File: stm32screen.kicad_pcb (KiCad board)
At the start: 4 copper layers, 49.8 x 49.8 mm, 38 parts, among them J1 SWD, J2 GC9A01, J3 Oil temp sensor, J4 pressure sensor, J5 USB_B_Micro, J6 EGT_sensor, SW1 SW_Push, SW2 SW_Push, U1 TS1117BCW-3.3, U2 STM32F407VETx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

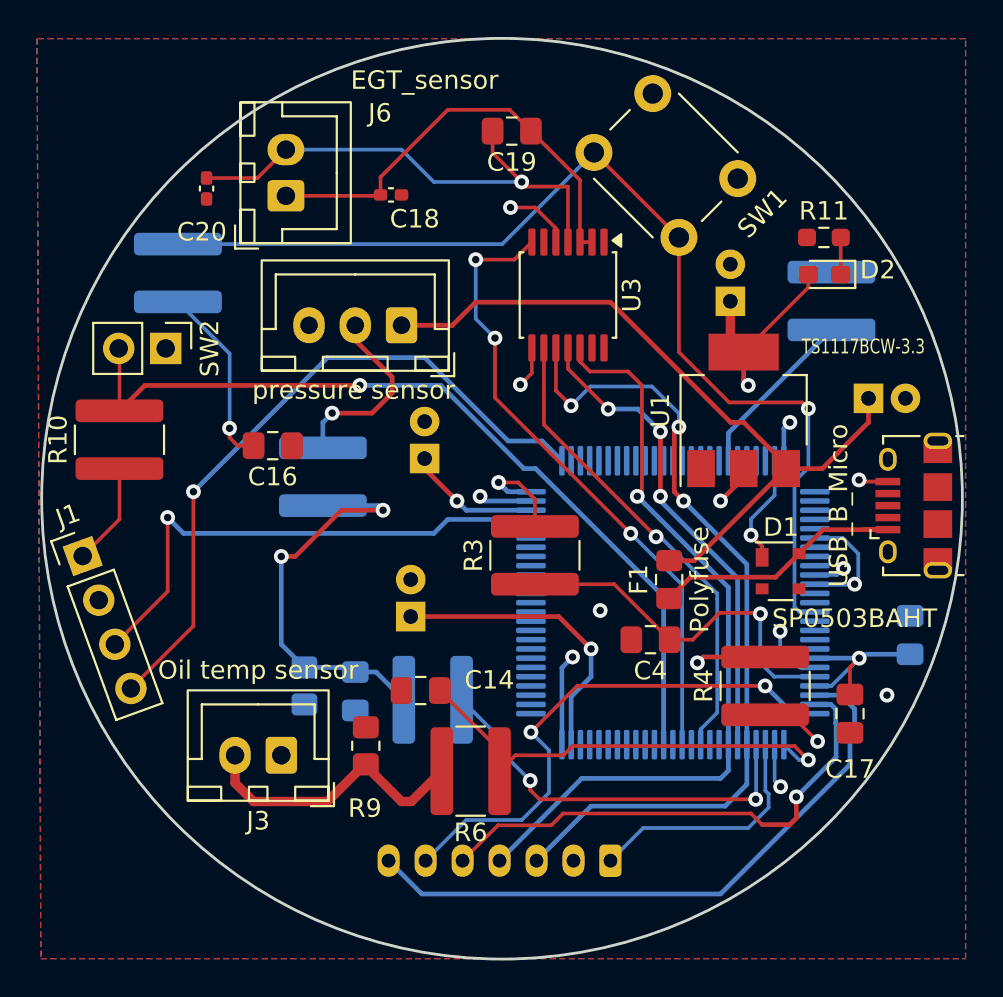
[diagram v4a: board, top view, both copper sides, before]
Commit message: Changed PCB size to 23mm radius, rearranged parts to fit
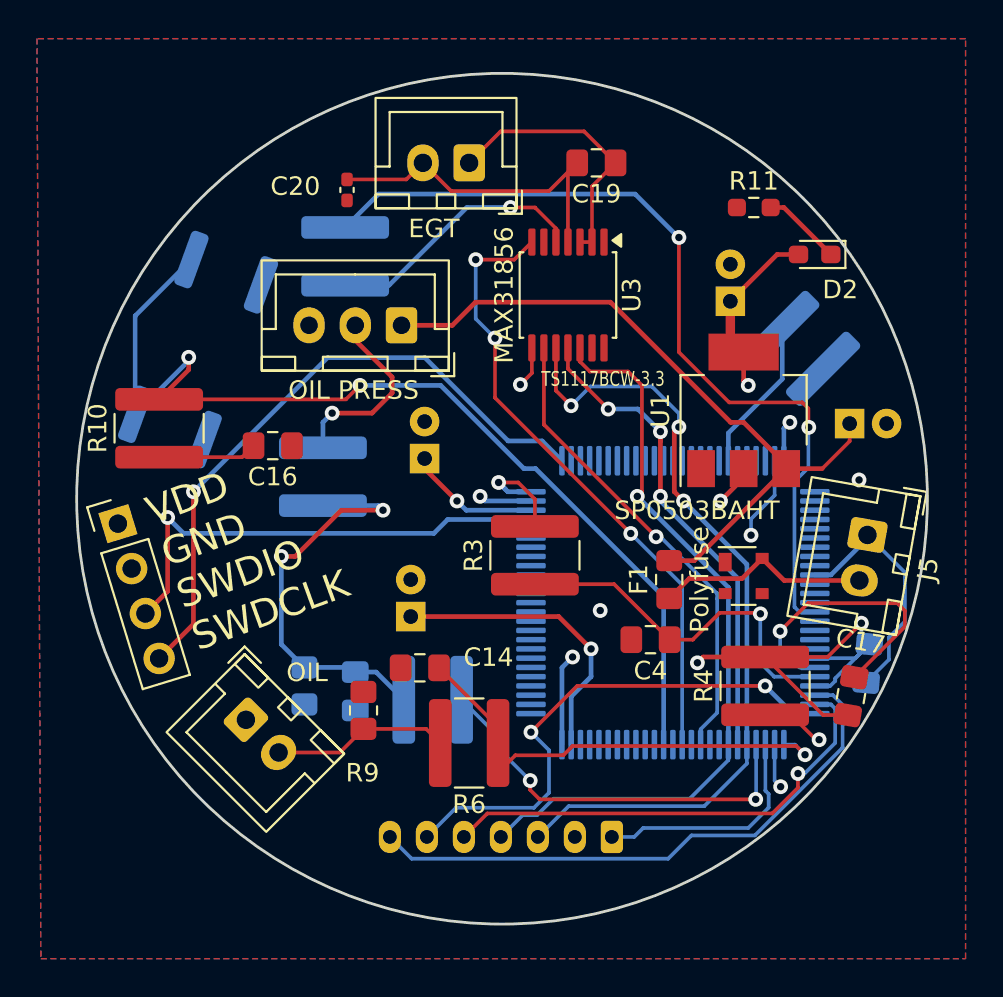
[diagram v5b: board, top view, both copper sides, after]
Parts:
- removed C18: 0.01uF, Capacitor_SMD:C_0402_1005Metric_Pad0.74x0.62mm_HandSolder
- removed SW1: SW_Push, Button_Switch_THT:SW_PUSH_6mm
- J3: value Oil temp sensor -> OIL
- J4: value pressure sensor -> OIL PRESS
- J5: value USB_B_Micro -> POWER IN; footprint Connector_USB:USB_Micro-B_Amphenol_10118194_Horizontal -> Connector_JST:JST_XH_B2B-XH-A_1x02_P2.50mm_Vertical
- J6: value EGT_sensor -> EGT
- SW2: footprint Connector_PinHeader_2.54mm:PinHeader_1x02_P2.54mm_Vertical -> Button_Switch_SMD:SW_Push_1P1T_NO_CK_KSC9xxG; moved to B.Cu
- moved J6 10.1 mm to (121.2, 53.5), turned to 180 degrees
- moved R1 9.09 mm to (114.5, 58.5)
- moved C20 7.59 mm to (114.6, 54.9)
- moved C19 4.89 mm to (128.0, 53.5)
- moved R11 4.12 mm to (136.5, 55.9)
- moved R2 3.00 mm to (139.2, 63.5), turned to 135 degrees
- moved J5 2.97 mm to (142.7, 73.6), turned to -100 degrees
- moved C13 2.75 mm to (142.7, 80.5), turned to 85 degrees
- moved J3 2.71 mm to (109.1, 83.6), turned to -45 degrees
- moved J1 2.59 mm to (102.2, 73.0), turned to 17 degrees
- moved R10 2.23 mm to (104.4, 67.8)
- moved D1 2.02 mm to (136.0, 75.8)
- moved R9 1.92 mm to (115.4, 83.1)
- moved SW2 1.75 mm to (106.5, 63.6), turned to 70 degrees
- moved C1 1.70 mm to (141.7, 67.6)
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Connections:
- D1 pad 4: Net-(J5-VBUS) -> Net-(J5-Pin_2)
- F1 pad 1: Net-(J5-VBUS) -> Net-(J5-Pin_2)
- J5 pad 1: Net-(J5-VBUS) -> GND
- J5 pad 2: unconnected-(J5-D--Pad2) -> Net-(J5-Pin_2)
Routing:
- net GND: track 17.8 -> 39.1 mm, vias 8 -> 6
- net Net-(J5-VBUS): track 14.6 -> 0.00 mm
- net Net-(J5-Pin_2): track 0.00 -> 11.7 mm
- net NRST: track 57.8 -> 46.4 mm, vias 1 -> 2
- net Net-(U2-PE8): track 46.1 -> 57.2 mm, vias 1 -> 2
- net Net-(J6-Pin_1): track 24.1 -> 14.8 mm
- net Net-(J6-Pin_2): track 27.4 -> 18.6 mm, vias 1 -> 0
- net Net-(J3-Pin_2): track 15.4 -> 9.58 mm
- net VDD: track 85.1 -> 87.8 mm, vias 12 -> 10
- net /RESET: track 34.2 -> 31.5 mm
- net /SWDIO: track 28.3 -> 26.0 mm
- net Net-(D2-K): track 2.00 -> 4.31 mm
- net /SWCLK: track 37.3 -> 35.0 mm
- net /D/C: track 27.5 -> 25.7 mm
- net Vin: track 40.3 -> 38.5 mm
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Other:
- board size 49.8 x 49.8 mm -> 46 x 46 mm
- board text added: "VDD GND SWDIO SWDCLK"

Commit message: Connected a couple of unconnected pads
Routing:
- net VDD: track 87.8 -> 100.4 mm
- net GND: track 39.1 -> 41.2 mm
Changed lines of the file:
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@@
+	)
+	(segment
+		(start 135.001 74.999)
+		(end 136.4 73.6)
+		(width 0.2)
+		(layer "F.Cu")
+		(net 2)
+	)
+	(segment
+		(start 135.001 75.057)
+		(end 135.001 74.999)
+		(width 0.2)
+		(layer "F.Cu")
+		(net 2)
 	)
 	(segment
@@
 	)
 	(segment
+		(start 102.166128 72.976957)
+		(end 104.394 70.749085)
+		(width 0.2)
+		(layer "F.Cu")
+		(net 5)
+	)
+	(segment
 		(start 133.813 80.187)
 		(end 133.5 80.5)
@@
 	)
 	(segment
+		(start 104.394 70.749085)
+		(end 104.394 69.3805)
+		(width 0.2)
+		(layer "F.Cu")
+		(net 5)
+	)
+	(segment
 		(start 123.8106 70.75)
 		(end 122.75 70.75)
@@
 	)
 	(segment
+		(start 139.016176 73.75)
+		(end 139.85 73.75)
+		(width 0.2)
+		(layer "B.Cu")
+		(net 5)
+	)
+	(segment
+		(start 138.749 74.017176)
+		(end 139.016176 73.75)
+		(width 0.2)
+		(layer "B.Cu")
+		(net 5)
+	)
+	(segment
+		(start 139.85 76.25)
+		(end 139.016176 76.25)
+		(width 0.2)
+		(layer "B.Cu")
+		(net 5)
+	)
+	(segment
 		(start 137.175 87.415636)
 		(end 137.353 87.593636)
@@
 		(start 140.683824 81.75)
 		(end 139.85 81.75)
+		(width 0.2)
+		(layer "B.Cu")
+		(net 5)
+	)
+	(segment
+		(start 142.367 77.933176)
+		(end 142.367 78.359)
 		(width 0.2)
 		(layer "B.Cu")
@@
 	)
 	(segment
+		(start 140.683824 76.25)
+		(end 142.367 77.933176)
+		(width 0.2)
+		(layer "B.Cu")
+		(net 5)
+	)
+	(segment
 		(start 126.175 84.925)
 		(end 126.175 80.762)
 		(width 0.254)
+		(layer "B.Cu")
+		(net 5)
+	)
+	(segment
+		(start 138.749 75.982824)
+		(end 138.749 74.017176)
+		(width 0.2)
 		(layer "B.Cu")
 		(net 5)
@@
 	)
 	(segment
+		(start 139.016176 76.25)
+		(end 138.749 75.982824)
+		(width 0.2)
+		(layer "B.Cu")
+		(net 5)
+	)
+	(segment
+		(start 139.85 76.25)
+		(end 140.683824 76.25)
+		(width 0.2)
+		(layer "B.Cu")
+		(net 5)
+	)
+	(segment
 		(start 132 79.25)
 		(end 129.0008 76.2508)
@@
 	)
 	(segment
+		(start 139.016176 77.75)
+		(end 138.348 77.081824)
+		(width 0.2)
+		(layer "B.Cu")
+		(net 11)
+	)
+	(segment
+		(start 139.5 69.9484)
+		(end 139.5 67.7894)
+		(width 0.2)
+		(layer "B.Cu")
+		(net 11)
+	)
+	(segment
+		(start 138.348 71.1004)
+		(end 139.5 69.9484)
+		(width 0.2)
+		(layer "B.Cu")
+		(net 11)
+	)
+	(segment
 		(start 139.5 67.7894)
 		(end 139.5222 67.7672)
@@
 	)
 	(segment
-		(start 138.749 70.6994)
-		(end 139.5 69.9484)
-		(width 0.2)
-		(layer "B.Cu")
-		(net 11)
-	)
-	(segment
-		(start 138.749 77.482824)
-		(end 138.749 70.6994)
+		(start 138.348 77.081824)
+		(end 138.348 71.1004)
 		(width 0.2)
 		(layer "B.Cu")
@@
 		(layer "B.Cu")
 		(net 11)
-	)
-	(segment
-		(start 139.5 69.9484)
-		(end 139.5 67.7894)
-		(width 0.2)
-		(layer "B.Cu")
-		(net 11)
-	)
-	(segment
-		(start 139.016176 77.75)
-		(end 138.749 77.482824)
-		(width 0.2)
-		(layer "B.Cu")
-		(net 11)
